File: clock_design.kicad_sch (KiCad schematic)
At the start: 28 parts, among them J1 Power_inlet_vertical, U1 ATmega328-PU, U2 L7805, U3 DS1307_DIP-8, Y1 Crystal_16MHz, Y2 Crystal_32768Hz

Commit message: Added new BOM (a single LED + resistor).
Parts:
- added D?: LED_0805_GRN, footprints:LED_0805_2012Metric, symbol HPS:LED_0805_GRN
- added R?: R_0805_2.2K, footprints:R_0805_2012Metric, symbol HPS:R_0805_2.2K
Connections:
- net GND: now also D?.1 (K)
- net SPI_SCLK: now also R?.1
- new net: D?.2 (A), R?.2
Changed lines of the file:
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@@
+    (stroke (width 0) (type default) (color 0 0 0 0))
+  )
+  (wire (pts (xy 139.7 123.19) (xy 139.7 128.27))
     (stroke (width 0) (type default) (color 0 0 0 0))
   )
@@
     (stroke (width 0) (type default) (color 0 0 0 0))
   )
+  (wire (pts (xy 139.7 115.57) (xy 139.7 111.76))
+    (stroke (width 0) (type default) (color 0 0 0 0))
+  )
   (wire (pts (xy 66.04 142.24) (xy 69.85 142.24))
     (stroke (width 0) (type default) (color 0 0 0 0))
@@
     (stroke (width 0) (type default) (color 0 0 0 0))
   )
+  (wire (pts (xy 139.7 111.76) (xy 135.89 111.76))
+    (stroke (width 0) (type default) (color 0 0 0 0))
+  )
   (wire (pts (xy 88.9 115.57) (xy 88.9 116.84))
     (stroke (width 0) (type default) (color 0 0 0 0))
@@
   )
   (wire (pts (xy 50.8 80.01) (xy 58.42 80.01))
+    (stroke (width 0) (type default) (color 0 0 0 0))
+  )
+  (wire (pts (xy 139.7 135.89) (xy 139.7 139.7))
     (stroke (width 0) (type default) (color 0 0 0 0))
   )
@@
     )
   )
+  (global_label "SPI_SCLK" (shape input) (at 135.89 111.76 180) (fields_autoplaced)
+    (effects (font (size 1.27 1.27) italic) (justify right))
+    (property "Intersheet References" "${INTERSHEET_REFS}" (id 0) (at 124.3918 111.6806 0)
+      (effects (font (size 1.27 1.27) italic) (justify right) hide)
+    )
+  )
   (global_label "SPI_SCLK" (shape output) (at 69.85 116.84 0) (fields_autoplaced)
     (effects (font (size 1.27 1.27) italic) (justify left))
@@
     (pin "1")
     (pin "2")
+  )
+  (symbol (lib_id "HPS:GND") (at 139.7 139.7 0) (unit 1)
+    (in_bom yes) (on_board yes) (fields_autoplaced)
+    (property "Reference" "#PWR?" (id 0) (at 139.7 146.05 0)
+      (effects (font (size 1.27 1.27)) hide)
+    )
+    (property "Value" "GND" (id 1) (at 139.7 144.78 0)
+      (effects (font (size 1.27 1.27)) hide)
+    )
+    (property "Footprint" "" (id 2) (at 139.7 139.7 0)
+      (effects (font (size 1.27 1.27)) hide)
+    )
+    (property "Datasheet" "" (id 3) (at 139.7 139.7 0)
+      (effects (font (size 1.27 1.27)) hide)
+    )
+    (pin "1")
   )
   (symbol (lib_id "HPS:GND") (at 40.64 52.07 0) (unit 1)
@@
     (pin "2")
   )
+  (symbol (lib_id "HPS:LED_0805_GRN") (at 139.7 132.08 90) (unit 1)
+    (in_bom yes) (on_board yes) (fields_autoplaced)
+    (property "Reference" "D?" (id 0) (at 143.51 132.4101 90)
+      (effects (font (size 1.27 1.27)) (justify right))
+    )
+    (property "Value" "LED_0805_GRN" (id 1) (at 143.51 134.9501 90)
+      (effects (font (size 1.27 1.27)) (justify right))
+    )
+    (property "Footprint" "footprints:LED_0805_2012Metric" (id 2) (at 151.13 130.81 0)
+      (effects (font (size 1.27 1.27)) hide)
+    )
+    (property "Datasheet" "https://www.we-online.com/katalog/datasheet/150080VS75000.pdf" (id 3) (at 139.7 132.08 0)
+      (effects (font (size 1.27 1.27)) hide)
+    )
+    (property "MFG" "Würth Elektronik" (id 4) (at 146.05 132.08 0)
+      (effects (font (size 1.27 1.27)) hide)
+    )
+    (property "MPN" "150080VS75000" (id 5) (at 148.59 132.08 0)
+      (effects (font (size 1.27 1.27)) hide)
+    )
+    (property "Digikey PN" "732-4986-1-ND" (id 6) (at 153.67 132.08 0)
+      (effects (font (size 1.27 1.27)) hide)
+    )
+    (property "Mouser PN" "N/A" (id 7) (at 156.21 132.08 0)
+      (effects (font (size 1.27 1.27)) hide)
+    )
+    (pin "1")
+    (pin "2")
+  )
   (symbol (lib_id "HPS:GND") (at 161.29 90.17 0) (unit 1)
     (in_bom yes) (on_board yes) (fields_autoplaced)
@@
     )
     (property "Tolerance" "N/A" (id 10) (at 210.82 160.02 0)
+      (effects (font (size 1.27 1.27)) hide)
+    )
+    (pin "1")
+    (pin "2")
+  )
+  (symbol (lib_id "HPS:R_0805_2.2K") (at 139.7 119.38 0) (unit 1)
+    (in_bom yes) (on_board yes) (fields_autoplaced)
+    (property "Reference" "R?" (id 0) (at 142.24 118.1099 0)
+      (effects (font (size 1.27 1.27)) (justify left))
+    )
+    (property "Value" "R_0805_2.2K" (id 1) (at 142.24 120.6499 0)
+      (effects (font (size 1.27 1.27)) (justify left))
+    )
+    (property "Footprint" "footprints:R_0805_2012Metric" (id 2) (at 135.382 119.38 90)
+      (effects (font (size 1.27 1.27)) hide)
+    )
+    (property "Datasheet" "https://www.digikey.com/en/products/detail/yageo/RC0805FR-072K2L/727676" (id 3) (at 137.16 119.38 0)
+      (effects (font (size 1.27 1.27)) hide)
+    )
+    (property "MFG" "N/A" (id 4) (at 139.7 125.73 0)
+      (effects (font (size 1.27 1.27)) hide)
+    )
+    (property "MPN" "N/A" (id 5) (at 139.7 128.27 0)
+      (effects (font (size 1.27 1.27)) hide)
+    )
+    (property "Digikey PN" "311-2.20KCRCT-ND" (id 6) (at 139.7 133.35 0)
+      (effects (font (size 1.27 1.27)) hide)
+    )
+    (property "Mouser PN" "N/A" (id 7) (at 139.7 135.89 0)
+      (effects (font (size 1.27 1.27)) hide)
+    )
+    (property "Power" "N/A" (id 8) (at 139.7 138.43 0)
+      (effects (font (size 1.27 1.27)) hide)
+    )
+    (property "Tolerance" "N/A" (id 9) (at 139.7 138.43 0)
       (effects (font (size 1.27 1.27)) hide)
     )
@@
       (reference "#PWR0136") (unit 1) (value "GND") (footprint "")
     )
+    (path "/1db71ecb-f082-4fe1-8e62-514bcfaa0e2d"
+      (reference "#PWR?") (unit 1) (value "GND") (footprint "")
+    )
     (path "/12399143-5f74-45ac-8086-3f780cf2c591"
       (reference "BT1") (unit 1) (value "Battery_Cell") (footprint "footprints:BatteryHolder_Keystone_106_1x20mm")
@@
       (reference "D3") (unit 1) (value "KWM-30881CVB") (footprint "footprints:KWM-30881CVB")
     )
+    (path "/6e5c2306-97c3-4235-b971-b2ebb60a6cd6"
+      (reference "D?") (unit 1) (value "LED_0805_GRN") (footprint "footprints:LED_0805_2012Metric")
+    )
     (path "/e73d99b1-0f17-4396-814b-a78c0ffe84da/8d63d620-db80-4923-8b2e-4dba06f0aba5"
       (reference "H1") (unit 1) (value "MountingHole") (footprint "footprints:MountingHole_3.2mm_M3")
@@
       (reference "R23") (unit 1) (value "R_0805_47") (footprint "footprints:R_0805_2012Metric")
     )
+    (path "/b5ae2498-fe7c-40d9-922a-566679c1819f"
+      (reference "R?") (unit 1) (value "R_0805_2.2K") (footprint "footprints:R_0805_2012Metric")
+    )
     (path "/1ded9e65-d766-4467-8652-a295879c8ab2/aa99d72d-ef0a-4c0c-95ca-bb3964a1ede7"

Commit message: Routing in progress...
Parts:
- gave numbers to parts that had none: 2
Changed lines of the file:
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@@
   (symbol (lib_id "HPS:GND") (at 139.7 139.7 0) (unit 1)
     (in_bom yes) (on_board yes) (fields_autoplaced)
-    (property "Reference" "#PWR?" (id 0) (at 139.7 146.05 0)
+    (property "Reference" "#PWR0124" (id 0) (at 139.7 146.05 0)
       (effects (font (size 1.27 1.27)) hide)
     )
@@
   (symbol (lib_id "HPS:LED_0805_GRN") (at 139.7 132.08 90) (unit 1)
     (in_bom yes) (on_board yes) (fields_autoplaced)
-    (property "Reference" "D?" (id 0) (at 143.51 132.4101 90)
+    (property "Reference" "D4" (id 0) (at 143.51 132.4101 90)
       (effects (font (size 1.27 1.27)) (justify right))
     )
@@
   (symbol (lib_id "HPS:R_0805_2.2K") (at 139.7 119.38 0) (unit 1)
     (in_bom yes) (on_board yes) (fields_autoplaced)
-    (property "Reference" "R?" (id 0) (at 142.24 118.1099 0)
+    (property "Reference" "R17" (id 0) (at 142.24 118.1099 0)
       (effects (font (size 1.27 1.27)) (justify left))
     )
@@
       (reference "#PWR0123") (unit 1) (value "GND") (footprint "")
     )
+    (path "/1db71ecb-f082-4fe1-8e62-514bcfaa0e2d"
+      (reference "#PWR0124") (unit 1) (value "GND") (footprint "")
+    )
     (path "/398dcb48-e636-4c28-8701-b4906ea4df14/dba4083a-e1a5-423f-9fef-86e5703e621a"
       (reference "#PWR0125") (unit 1) (value "GND") (footprint "")
@@
       (reference "#PWR0136") (unit 1) (value "GND") (footprint "")
     )
-    (path "/1db71ecb-f082-4fe1-8e62-514bcfaa0e2d"
-      (reference "#PWR?") (unit 1) (value "GND") (footprint "")
-    )
     (path "/12399143-5f74-45ac-8086-3f780cf2c591"
       (reference "BT1") (unit 1) (value "Battery_Cell") (footprint "footprints:BatteryHolder_Keystone_106_1x20mm")
@@
     )
     (path "/6e5c2306-97c3-4235-b971-b2ebb60a6cd6"
-      (reference "D?") (unit 1) (value "LED_0805_GRN") (footprint "footprints:LED_0805_2012Metric")
+      (reference "D4") (unit 1) (value "LED_0805_GRN") (footprint "footprints:LED_0805_2012Metric")
     )
     (path "/e73d99b1-0f17-4396-814b-a78c0ffe84da/8d63d620-db80-4923-8b2e-4dba06f0aba5"
@@
       (reference "R16") (unit 1) (value "R_0805_22K") (footprint "footprints:R_0805_2012Metric")
     )
+    (path "/b5ae2498-fe7c-40d9-922a-566679c1819f"
+      (reference "R17") (unit 1) (value "R_0805_2.2K") (footprint "footprints:R_0805_2012Metric")
+    )
     (path "/61bf49de-7bf3-4092-92f7-a9f338e64263/13c76214-6134-446b-8d07-3a965a1923e5"
       (reference "R18") (unit 1) (value "R_0805_22K") (footprint "footprints:R_0805_2012Metric")
@@
       (reference "R23") (unit 1) (value "R_0805_47") (footprint "footprints:R_0805_2012Metric")
     )
-    (path "/b5ae2498-fe7c-40d9-922a-566679c1819f"
-      (reference "R?") (unit 1) (value "R_0805_2.2K") (footprint "footprints:R_0805_2012Metric")
-    )
     (path "/1ded9e65-d766-4467-8652-a295879c8ab2/aa99d72d-ef0a-4c0c-95ca-bb3964a1ede7"

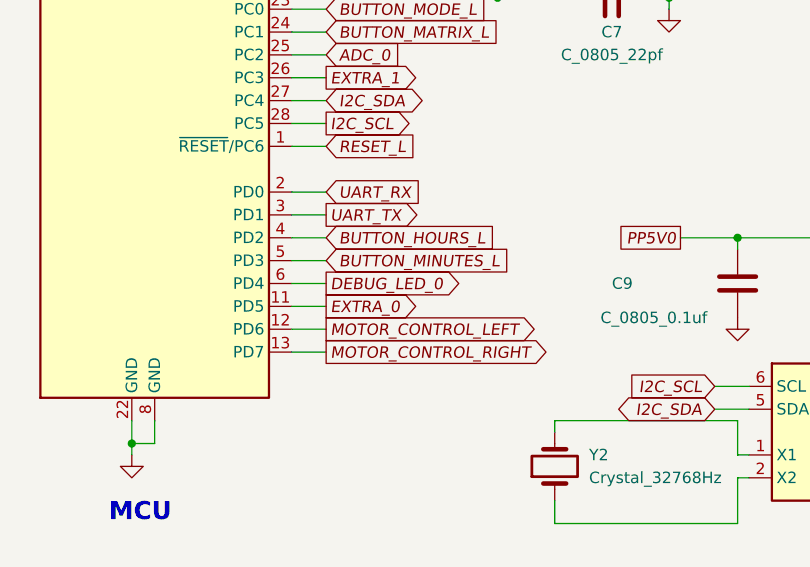
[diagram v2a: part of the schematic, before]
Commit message: Initial gerber out
Got all of the files for gereber out
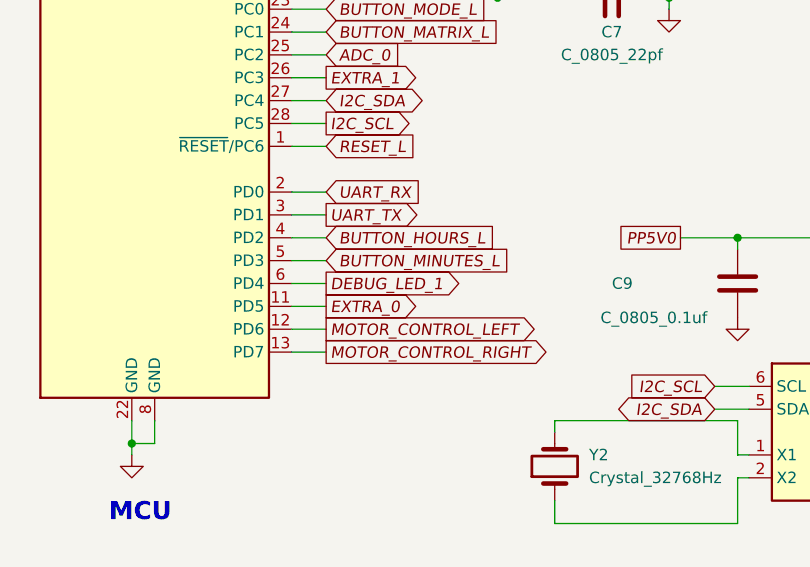
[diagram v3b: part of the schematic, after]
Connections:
- net DEBUG_LED_0: no longer U1.6 (PD4)
- net DEBUG_LED_1: now also U1.6 (PD4)
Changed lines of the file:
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@@
     )
   )
-  (global_label "DEBUG_LED_0" (shape output) (at 69.85 157.48 0) (fields_autoplaced)
+  (global_label "DEBUG_LED_1" (shape output) (at 69.85 157.48 0) (fields_autoplaced)
     (effects (font (size 1.27 1.27) italic) (justify left))
     (property "Intersheet References" "${INTERSHEET_REFS}" (id 0) (at 85.4001 157.4006 0)
@@
       (reference "TP2") (unit 1) (value "TestPoint") (footprint "footprints:TestPoint_THTPad_D2.0mm_Drill1.0mm")
     )
-    (path "/e73d99b1-0f17-4396-814b-a78c0ffe84da/6f095ff8-89d8-47b7-bf70-70b96455cf28"
-      (reference "TP3") (unit 1) (value "TestPoint") (footprint "footprints:TestPoint_THTPad_D2.0mm_Drill1.0mm")
-    )
-    (path "/e73d99b1-0f17-4396-814b-a78c0ffe84da/230e0172-3aea-4c9a-b894-ade73caea90c"
-      (reference "TP4") (unit 1) (value "TestPoint") (footprint "footprints:TestPoint_THTPad_D2.0mm_Drill1.0mm")
-    )
-    (path "/e73d99b1-0f17-4396-814b-a78c0ffe84da/acf742f7-4dbb-46da-a18b-c87bc15c7a0a"
-      (reference "TP5") (unit 1) (value "TestPoint") (footprint "footprints:TestPoint_THTPad_D2.0mm_Drill1.0mm")
-    )
-    (path "/e73d99b1-0f17-4396-814b-a78c0ffe84da/e181b7d9-f696-41e9-af2b-d5088ea78d91"
-      (reference "TP6") (unit 1) (value "TestPoint") (footprint "footprints:TestPoint_THTPad_D2.0mm_Drill1.0mm")
-    )
-    (path "/e73d99b1-0f17-4396-814b-a78c0ffe84da/0dd9a317-7931-40f0-809b-2d8c5309978c"
-      (reference "TP7") (unit 1) (value "TestPoint") (footprint "footprints:TestPoint_THTPad_D2.0mm_Drill1.0mm")
-    )
-    (path "/e73d99b1-0f17-4396-814b-a78c0ffe84da/5ad20c18-d3a3-40c0-91ad-ecad1064a8af"
-      (reference "TP8") (unit 1) (value "TestPoint") (footprint "footprints:TestPoint_THTPad_D2.0mm_Drill1.0mm")
-    )
-    (path "/e73d99b1-0f17-4396-814b-a78c0ffe84da/78246a38-335b-4eb6-a50d-47a42c39a108"
-      (reference "TP9") (unit 1) (value "TestPoint") (footprint "footprints:TestPoint_THTPad_D2.0mm_Drill1.0mm")
-    )
-    (path "/e73d99b1-0f17-4396-814b-a78c0ffe84da/aa7d6f72-f6af-4dd5-9537-95015a7af6c7"
-      (reference "TP10") (unit 1) (value "TestPoint") (footprint "footprints:TestPoint_THTPad_D2.0mm_Drill1.0mm")
-    )
-    (path "/e73d99b1-0f17-4396-814b-a78c0ffe84da/ed6d4011-33b4-4f43-bb79-36ce816ea052"
-      (reference "TP11") (unit 1) (value "TestPoint") (footprint "footprints:TestPoint_THTPad_D2.0mm_Drill1.0mm")
-    )
-    (path "/e73d99b1-0f17-4396-814b-a78c0ffe84da/ff928f2c-488e-49ae-880e-8e20cd3d8575"
-      (reference "TP12") (unit 1) (value "TestPoint") (footprint "footprints:TestPoint_THTPad_D2.0mm_Drill1.0mm")
-    )
-    (path "/e73d99b1-0f17-4396-814b-a78c0ffe84da/77840552-51c5-4f37-b046-0ca68df8cc21"
-      (reference "TP13") (unit 1) (value "TestPoint") (footprint "footprints:TestPoint_THTPad_D2.0mm_Drill1.0mm")
-    )
-    (path "/e73d99b1-0f17-4396-814b-a78c0ffe84da/49d4c9ff-f35a-48d9-aabd-2a8ad4d82ebb"
-      (reference "TP14") (unit 1) (value "TestPoint") (footprint "footprints:TestPoint_THTPad_D2.0mm_Drill1.0mm")
-    )
-    (path "/e73d99b1-0f17-4396-814b-a78c0ffe84da/41ed9bf5-dbf5-4b95-9d91-985c555c0fed"
-      (reference "TP15") (unit 1) (value "TestPoint") (footprint "footprints:TestPoint_THTPad_D2.0mm_Drill1.0mm")
-    )
-    (path "/e73d99b1-0f17-4396-814b-a78c0ffe84da/e09672a2-cfae-4465-afb9-66a3a11f74a9"
-      (reference "TP16") (unit 1) (value "TestPoint") (footprint "footprints:TestPoint_THTPad_D2.0mm_Drill1.0mm")
-    )
-    (path "/e73d99b1-0f17-4396-814b-a78c0ffe84da/9e2c471f-2559-4157-b751-d0d822cef252"
-      (reference "TP17") (unit 1) (value "TestPoint") (footprint "footprints:TestPoint_THTPad_D2.0mm_Drill1.0mm")
-    )
-    (path "/e73d99b1-0f17-4396-814b-a78c0ffe84da/7513c72b-885f-405c-8586-2dec0c6c1346"
-      (reference "TP18") (unit 1) (value "TestPoint") (footprint "footprints:TestPoint_THTPad_D2.0mm_Drill1.0mm")
-    )
-    (path "/e73d99b1-0f17-4396-814b-a78c0ffe84da/038fceb6-4e3b-4c47-8d8d-4a8a83e3b908"
-      (reference "TP19") (unit 1) (value "TestPoint") (footprint "footprints:TestPoint_THTPad_D2.0mm_Drill1.0mm")
-    )
-    (path "/e73d99b1-0f17-4396-814b-a78c0ffe84da/4743a689-1148-47d0-9861-65bfead59bfe"
-      (reference "TP20") (unit 1) (value "TestPoint") (footprint "footprints:TestPoint_THTPad_D2.0mm_Drill1.0mm")
-    )
-    (path "/e73d99b1-0f17-4396-814b-a78c0ffe84da/57335f5e-6acc-4605-80a9-ff8282204976"
-      (reference "TP21") (unit 1) (value "TestPoint") (footprint "footprints:TestPoint_THTPad_D2.0mm_Drill1.0mm")
-    )
     (path "/e73d99b1-0f17-4396-814b-a78c0ffe84da/dee72d4b-97fa-40ed-9288-9a36390b0b0c"
